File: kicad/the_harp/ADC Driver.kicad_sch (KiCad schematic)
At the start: 17 parts, among them U601 THS4522IPW

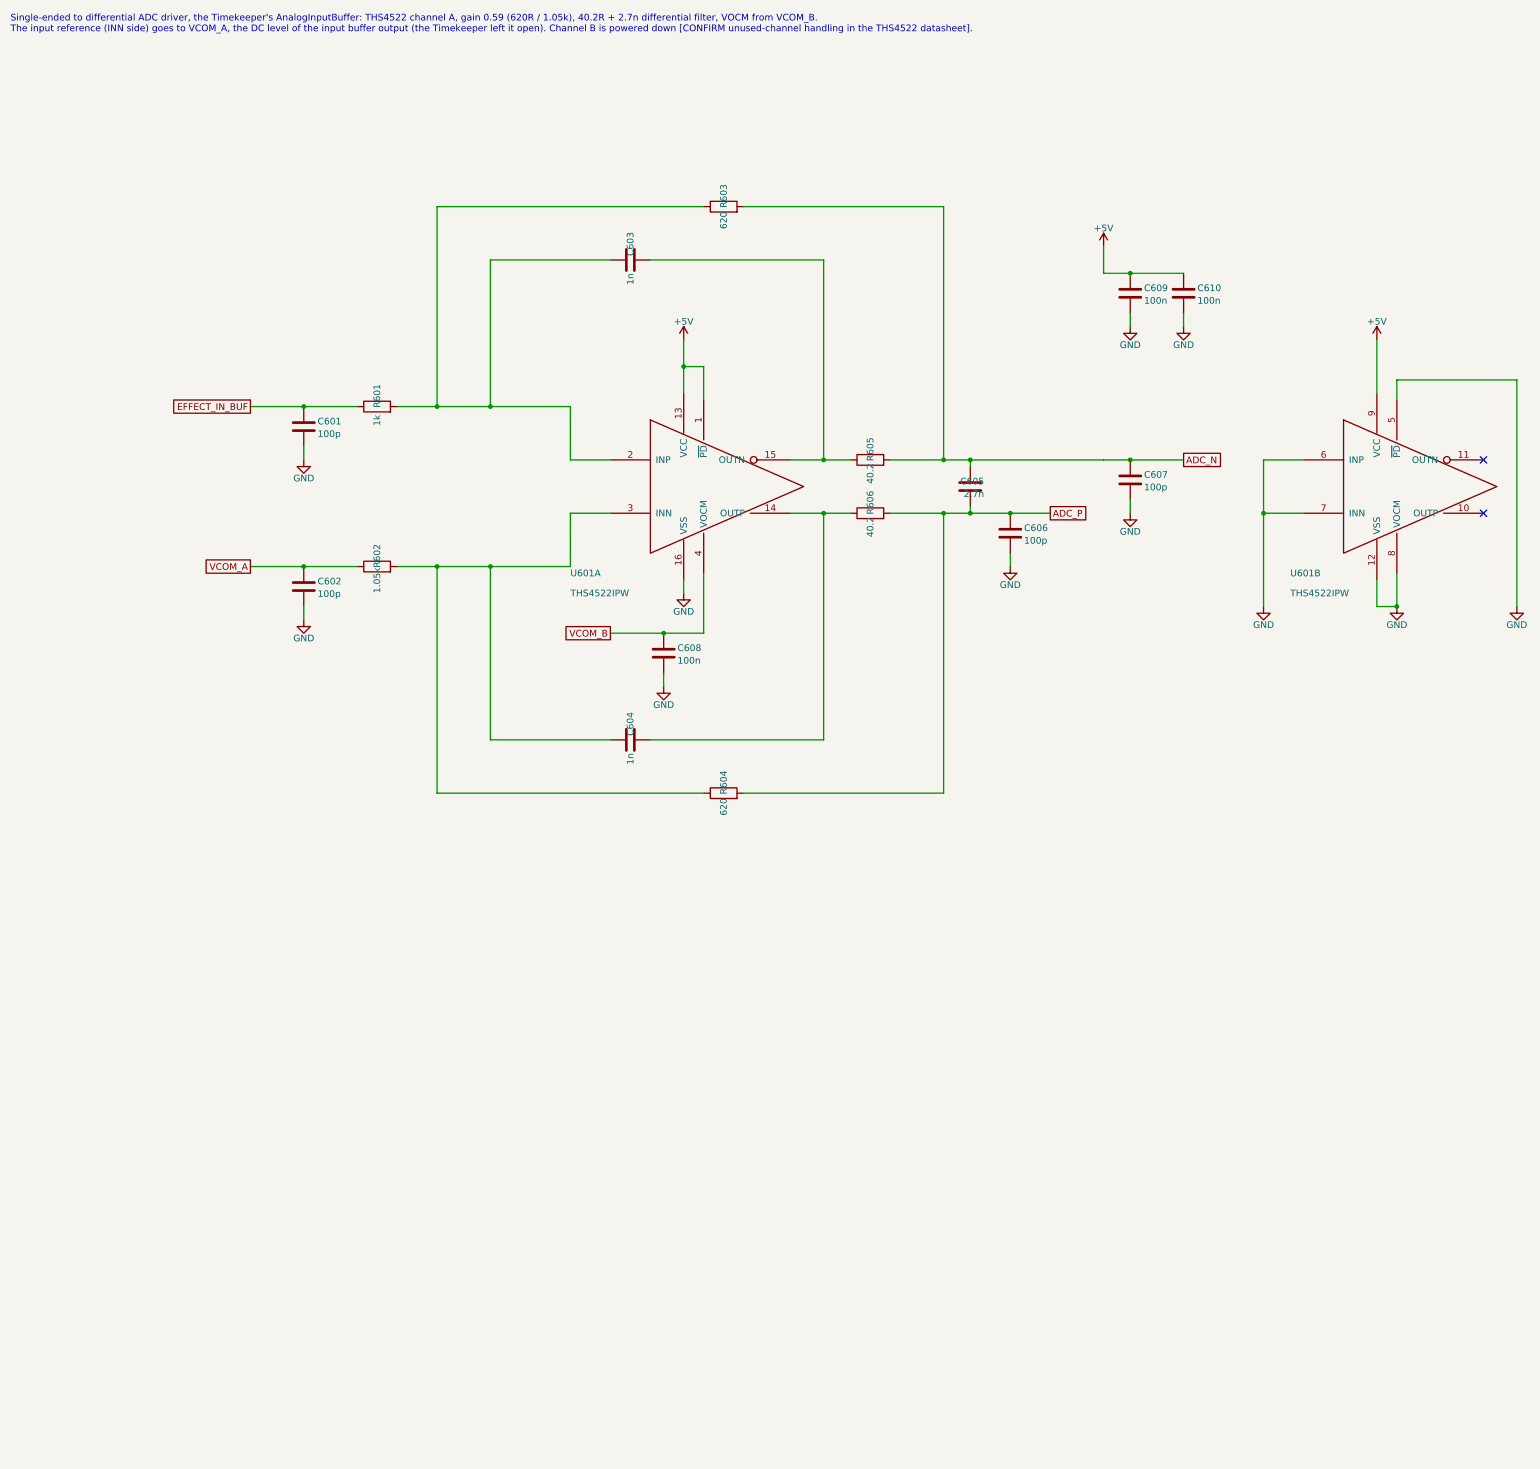
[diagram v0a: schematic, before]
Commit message: Stereo single-ended input and an OLED display
IN becomes a TRS jack (tip left, ring right) with a second OPA2365 buffer and
THS4522 channel B into the AK4621EF's AINR; the codec inputs are no longer
parked. A mono plug is detected by the right channel reading silence. The
twelve note LEDs and R107-R118 give way to a 0.91 in I2C OLED connector (J408,
PB6/PB7) with 4.7k pull-ups. Schematic regenerated (190 parts, netlist OK on
all sheets); design brief, PCB plan, firmware requirements and the design
report updated. The PCB still carries the old LED footprints until Update PCB
from Schematic is run in KiCad.

Co-Authored-By: Claude Sonnet 5.5 <noreply@anthropic.com>
Claude-Session: https://claude.ai/code/session_016hDejPHPgG8auBLMyByYZK
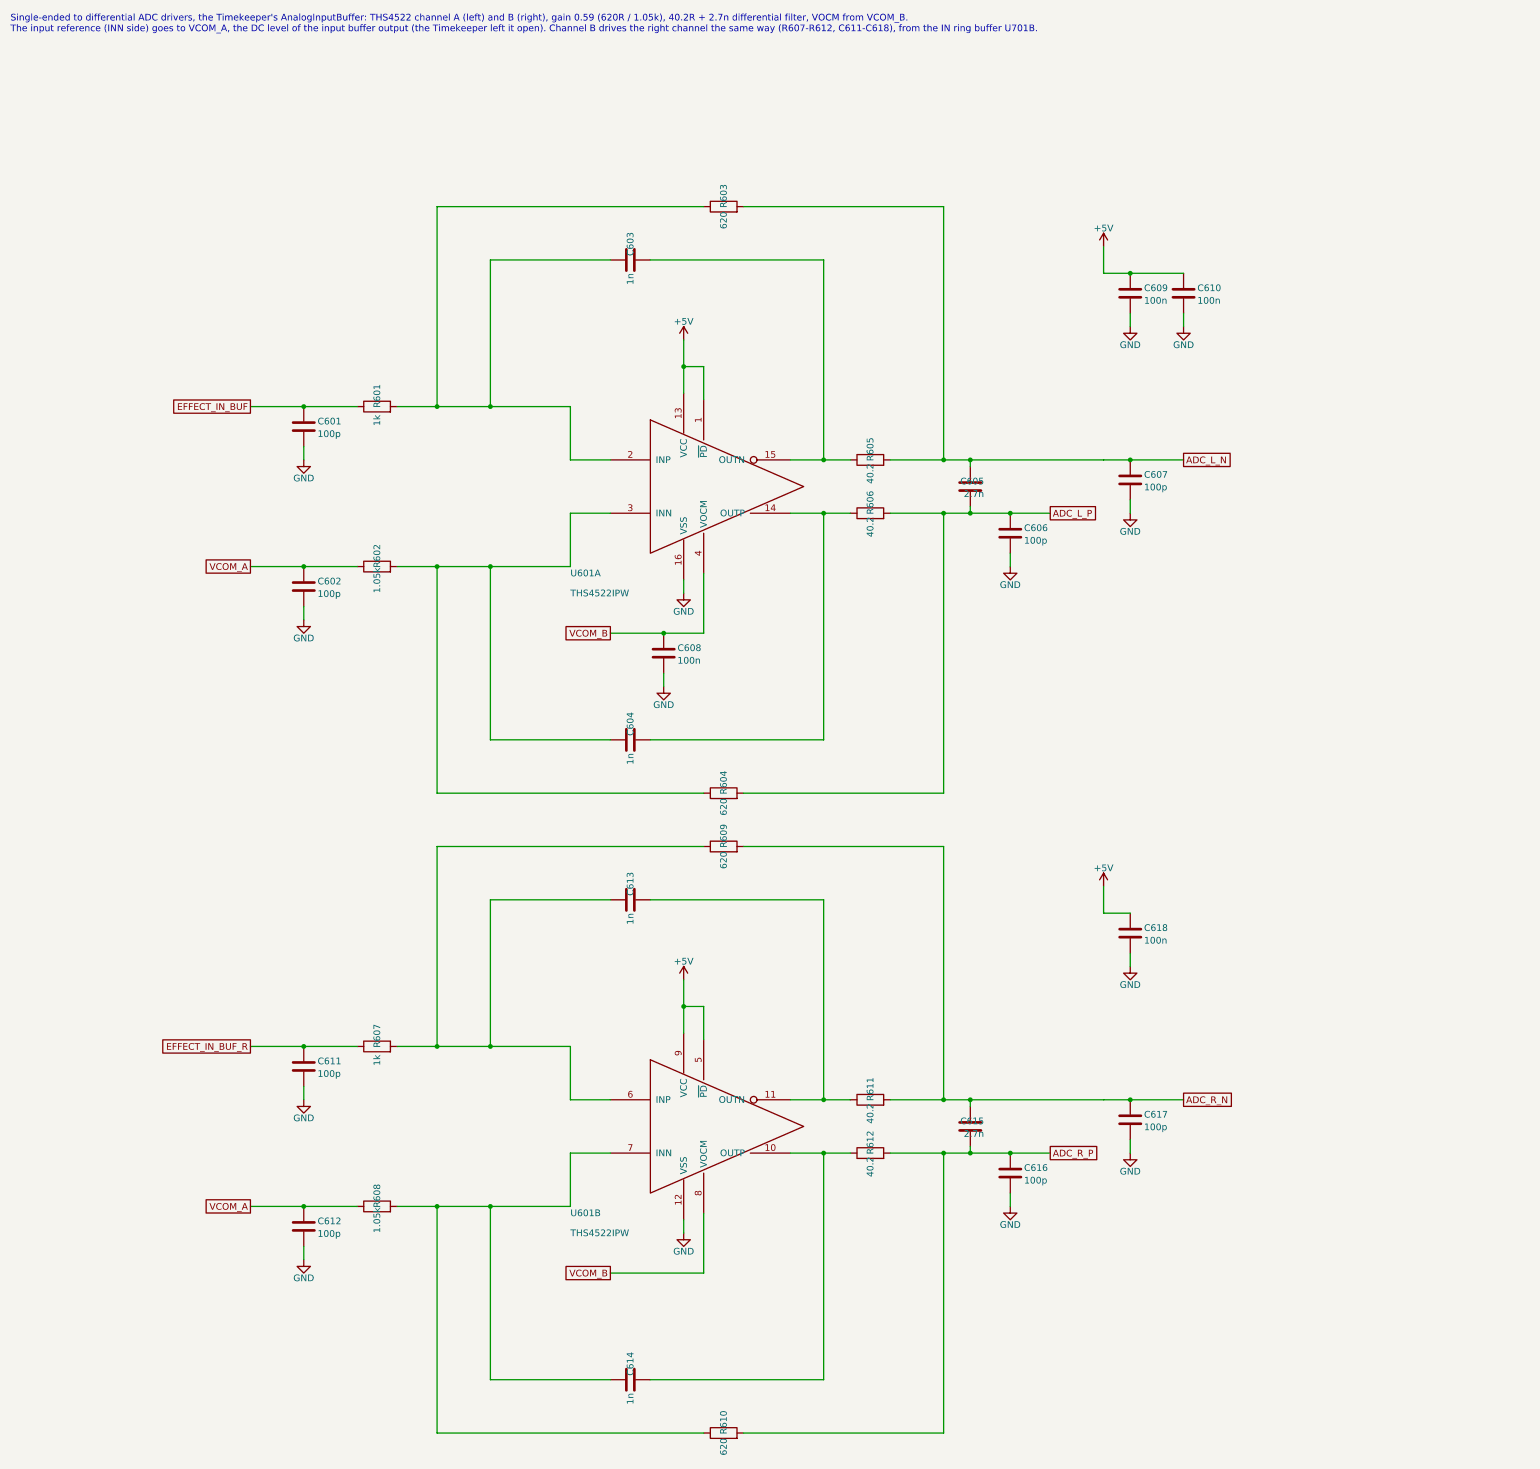
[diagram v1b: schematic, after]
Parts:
- added C611, C612, C616, C617: 100p, Capacitor_SMD:C_0603_1608Metric, symbol Device:C
- added C613, C614: 1n, Capacitor_SMD:C_0603_1608Metric, symbol Device:C
- added C615: 2.7n, Capacitor_SMD:C_0603_1608Metric, symbol Device:C
- added C618: 100n, Capacitor_SMD:C_0603_1608Metric, symbol Device:C
- added R607: 1k, Resistor_SMD:R_0603_1608Metric, symbol Device:R
- added R608: 1.05k, Resistor_SMD:R_0603_1608Metric, symbol Device:R
- added R609, R610: 620, Resistor_SMD:R_0603_1608Metric, symbol Device:R
- added R611, R612: 40.2, Resistor_SMD:R_0603_1608Metric, symbol Device:R
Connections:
- net +5V: now also U601.5 (~{PD}), C618.1
- net GND: now also C611.2, C612.2, C616.2, C617.2, C618.2; no longer U601.5 (~{PD}), U601.6 (INP), U601.7 (INN), U601.8 (VOCM)
- net VCOM_A: now also C612.1, R608.1
- net VCOM_B: now also U601.8 (VOCM)
- net at U601.10 (OUTP): now also C614.2, R612.1
- net at U601.11 (OUTN): now also C613.2, R611.1
- net ADC_N renamed ADC_L_N
- net ADC_P renamed ADC_L_P
- new net: C614.1, R608.2, R610.1, U601.7 (INN)
- new net: C613.1, R607.2, R609.1, U601.6 (INP)
- new net ADC_R_N: C615.2, C617.1, R609.2, R611.2
- new net ADC_R_P: C615.1, C616.1, R610.2, R612.2
- new net EFFECT_IN_BUF_R: C611.1, R607.1
- no-connect marks 2 -> 0
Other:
- note added: "Single-ended to differential ADC drivers, the Timekeeper's AnalogInputBuffer: THS4522 channel A (left) and B (right), gain 0.59 (620R / 1.05k), 40.2R + 2.7n differential filter, VOCM from VCOM_B. The input reference (INN side) goes to VCOM_A, the DC level of the input buffer output (the Timekeeper left it open). Channel B drives the right channel the same way (R607-R612, C611-C618), from the IN r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"
- note removed: "Single-ended to differential ADC driver, the Timekeeper's AnalogInputBuffer: THS4522 channel A, gain 0.59 (620R / 1.05k), 40.2R + 2.7n differential filter, VOCM from VCOM_B. The input reference (INN side) goes to VCOM_A, the DC level of the input buffer output (the Timekeeper left it open). Channel B is powered down [CONFIRM unused-channel handling in the THS4522 datasheet]."
- moved on the sheet: U601B
